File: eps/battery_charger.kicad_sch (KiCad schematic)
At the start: 25 parts, among them Q1 BSC028N06LS3, Q3 NMOS, U2 LTC4359-MS8, U4 BQ25185, U6 LTC4015EUHF_TRPBF

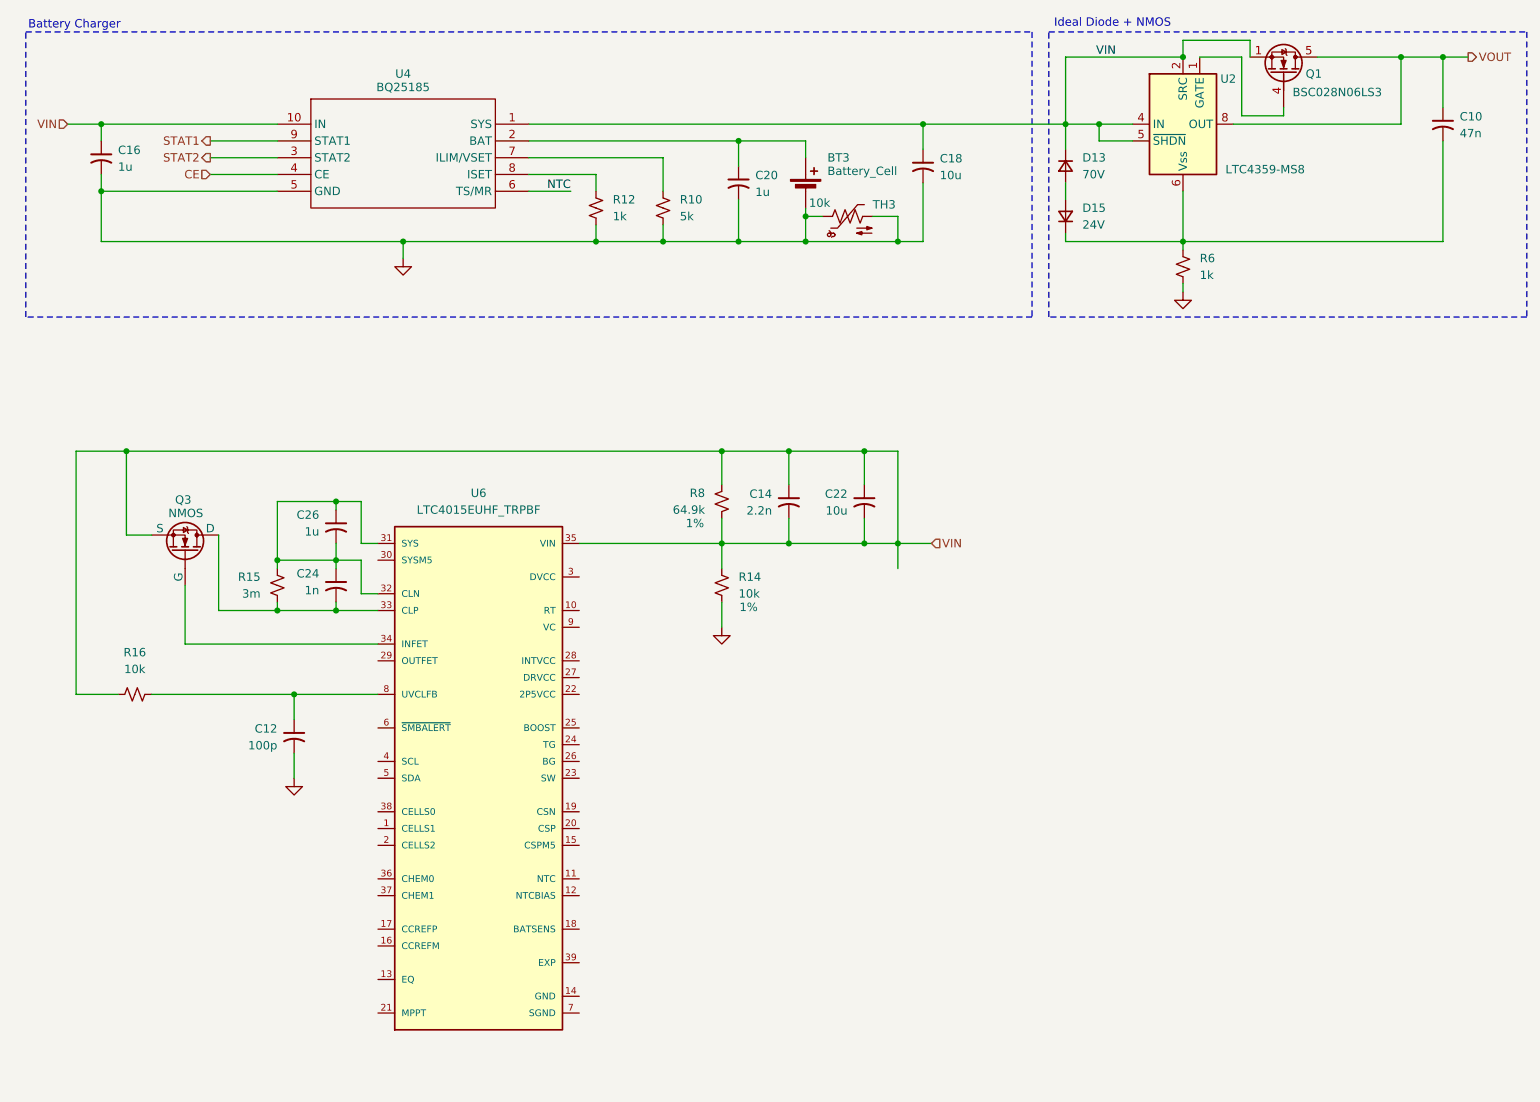
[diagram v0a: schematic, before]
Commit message: add custom symbol for ltc4015
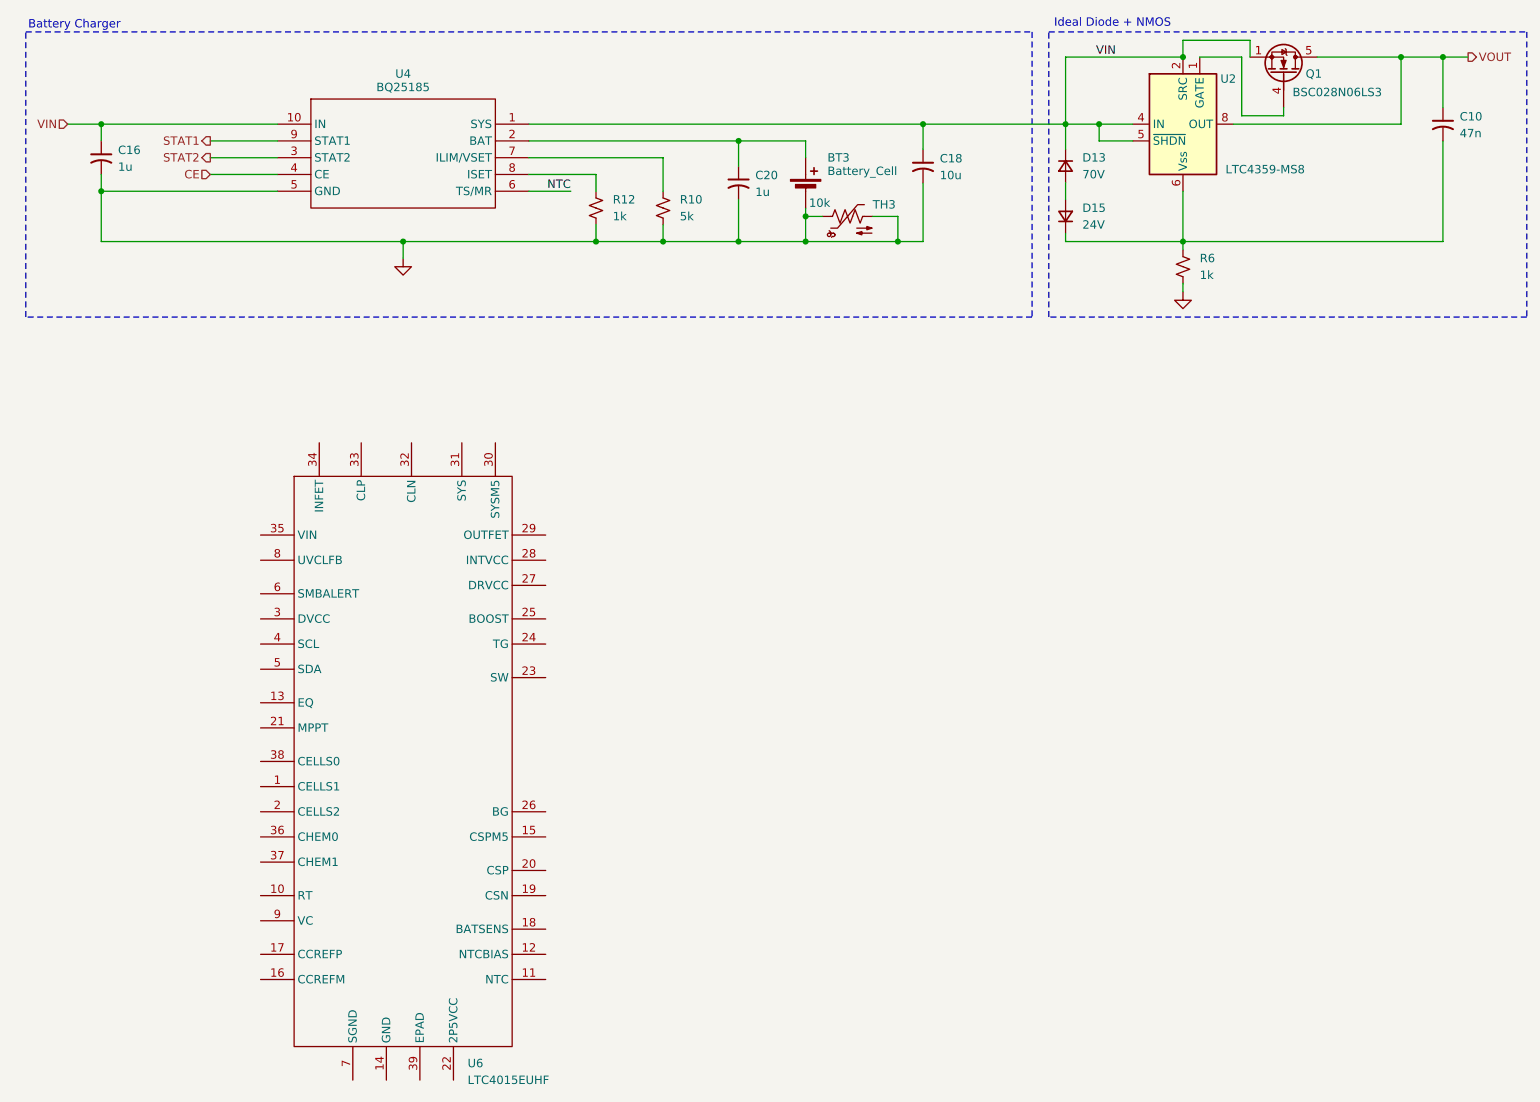
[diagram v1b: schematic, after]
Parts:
- removed C12: 100p, symbol Device:C_Small_US
- removed C14: 2.2n, symbol Device:C_Small_US
- removed C22: 10u, symbol Device:C_Small_US
- removed C24: 1n, symbol Device:C_Small_US
- removed C26: 1u, symbol Device:C_Small_US
- removed Q3: NMOS, symbol Simulation_SPICE:NMOS
- removed R14, R16: 10k, symbol Device:R_Small_US
- removed R15: 3m, symbol Device:R_Small_US
- removed R8: 64.9k, symbol Device:R_Small_US
- removed U6: LTC4015EUHF_TRPBF, LTC4015EUHF_TRPBF:QFN50P700X500X80-39N, symbol LTC4015EUHF_TRPBF:LTC4015EUHF_TRPBF
- added U6: LTC4015EUHF, symbol LTC4015:LTC4015EUHF
